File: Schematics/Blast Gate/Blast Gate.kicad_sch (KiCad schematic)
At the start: 14 parts

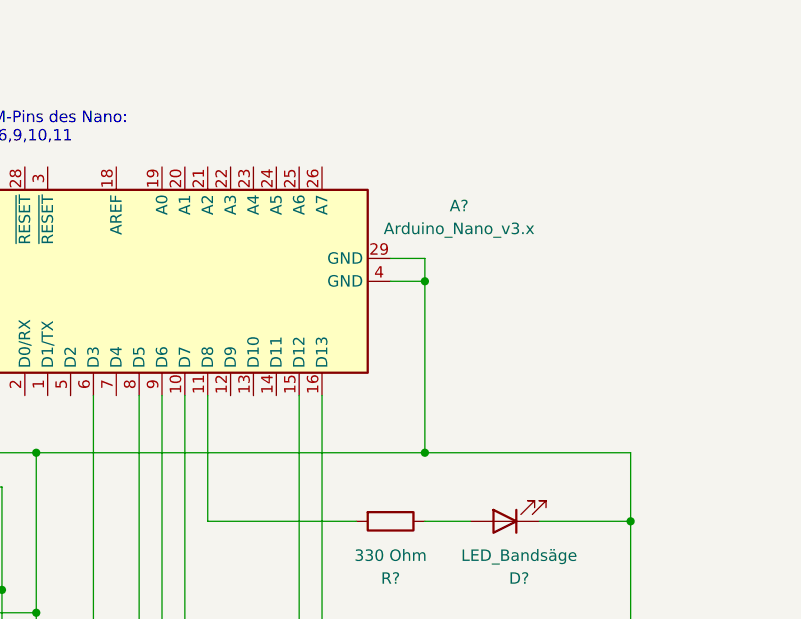
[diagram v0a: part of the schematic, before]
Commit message: Add buttons for open/close, introduced basic logic
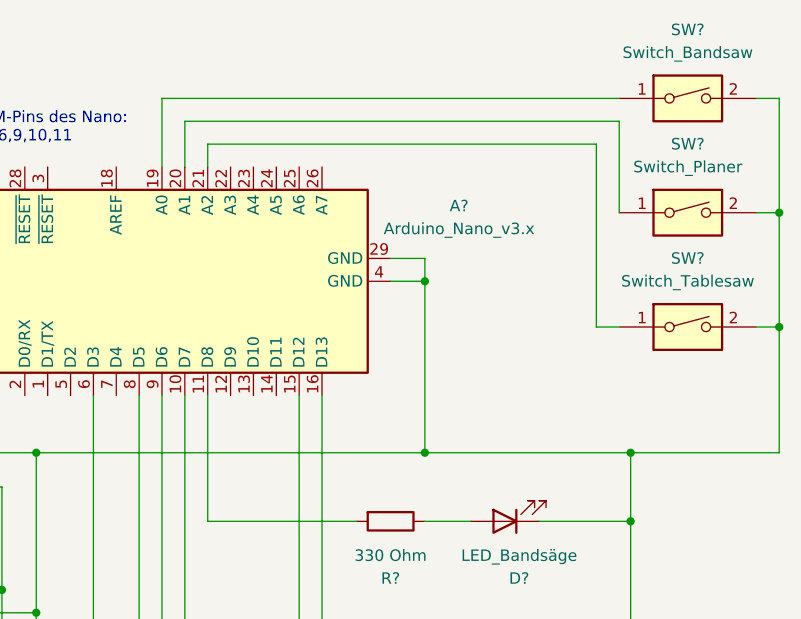
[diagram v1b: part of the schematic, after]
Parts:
- added SW?: Switch_Tablesaw, symbol Switch:SW_DIP_x01
- added SW?: Switch_Bandsaw, symbol Switch:SW_DIP_x01
- added SW?: Switch_Planer, symbol Switch:SW_DIP_x01
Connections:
- net GND: now also SW?.2, SW?.2, SW?.2
- net at A?.19 (A0): now also SW?.1
- net at A?.20 (A1): now also SW?.1
- net at A?.21 (A2): now also SW?.1
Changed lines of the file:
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@@
   (junction (at 86.36 107.95) (diameter 0) (color 0 0 0 0)
   )
+  (junction (at 168.91 48.26) (diameter 0) (color 0 0 0 0)
+  )
   (junction (at 55.88 52.07) (diameter 0) (color 0 0 0 0)
   )
@@
   (junction (at 41.91 104.14) (diameter 0) (color 0 0 0 0)
   )
+  (junction (at 168.91 35.56) (diameter 0) (color 0 0 0 0)
+  )
   (junction (at 82.55 105.41) (diameter 0) (color 0 0 0 0)
   )
+  (junction (at 152.4 62.23) (diameter 0) (color 0 0 0 0)
+  )
   (junction (at 86.36 80.01) (diameter 0) (color 0 0 0 0)
   )
@@
     (stroke (width 0) (type default) (color 0 0 0 0))
   )
+  (wire (pts (xy 100.33 30.48) (xy 100.33 22.86))
+    (stroke (width 0) (type default) (color 0 0 0 0))
+  )
   (wire (pts (xy 30.48 99.06) (xy 36.83 99.06))
     (stroke (width 0) (type default) (color 0 0 0 0))
@@
     (stroke (width 0) (type default) (color 0 0 0 0))
   )
+  (wire (pts (xy 168.91 62.23) (xy 152.4 62.23))
+    (stroke (width 0) (type default) (color 0 0 0 0))
+  )
   (wire (pts (xy 82.55 77.47) (xy 82.55 91.44))
     (stroke (width 0) (type default) (color 0 0 0 0))
@@
     (stroke (width 0) (type default) (color 0 0 0 0))
   )
+  (wire (pts (xy 166.37 48.26) (xy 168.91 48.26))
+    (stroke (width 0) (type default) (color 0 0 0 0))
+  )
   (wire (pts (xy 74.93 38.1) (xy 63.5 38.1))
     (stroke (width 0) (type default) (color 0 0 0 0))
@@
     (stroke (width 0) (type default) (color 0 0 0 0))
   )
+  (wire (pts (xy 168.91 48.26) (xy 168.91 62.23))
+    (stroke (width 0) (type default) (color 0 0 0 0))
+  )
   (wire (pts (xy 63.5 54.61) (xy 58.42 54.61))
     (stroke (width 0) (type default) (color 0 0 0 0))
@@
     (stroke (width 0) (type default) (color 0 0 0 0))
   )
+  (wire (pts (xy 151.13 25.4) (xy 151.13 35.56))
+    (stroke (width 0) (type default) (color 0 0 0 0))
+  )
   (wire (pts (xy 115.57 55.88) (xy 115.57 85.09))
     (stroke (width 0) (type default) (color 0 0 0 0))
@@
     (stroke (width 0) (type default) (color 0 0 0 0))
   )
+  (wire (pts (xy 102.87 25.4) (xy 151.13 25.4))
+    (stroke (width 0) (type default) (color 0 0 0 0))
+  )
   (wire (pts (xy 86.36 128.27) (xy 86.36 107.95))
     (stroke (width 0) (type default) (color 0 0 0 0))
   )
+  (wire (pts (xy 102.87 30.48) (xy 102.87 25.4))
+    (stroke (width 0) (type default) (color 0 0 0 0))
+  )
   (wire (pts (xy 82.55 77.47) (xy 82.55 66.04))
     (stroke (width 0) (type default) (color 0 0 0 0))
@@
     (stroke (width 0) (type default) (color 0 0 0 0))
   )
+  (wire (pts (xy 105.41 27.94) (xy 148.59 27.94))
+    (stroke (width 0) (type default) (color 0 0 0 0))
+  )
   (wire (pts (xy 152.4 85.09) (xy 152.4 69.85))
     (stroke (width 0) (type default) (color 0 0 0 0))
@@
     (stroke (width 0) (type default) (color 0 0 0 0))
   )
+  (wire (pts (xy 168.91 22.86) (xy 168.91 35.56))
+    (stroke (width 0) (type default) (color 0 0 0 0))
+  )
   (wire (pts (xy 142.24 69.85) (xy 152.4 69.85))
     (stroke (width 0) (type default) (color 0 0 0 0))
@@
     (stroke (width 0) (type default) (color 0 0 0 0))
   )
+  (wire (pts (xy 148.59 48.26) (xy 151.13 48.26))
+    (stroke (width 0) (type default) (color 0 0 0 0))
+  )
+  (wire (pts (xy 105.41 30.48) (xy 105.41 27.94))
+    (stroke (width 0) (type default) (color 0 0 0 0))
+  )
   (wire (pts (xy 78.74 80.01) (xy 86.36 80.01))
     (stroke (width 0) (type default) (color 0 0 0 0))
@@
     (stroke (width 0) (type default) (color 0 0 0 0))
   )
+  (wire (pts (xy 148.59 27.94) (xy 148.59 48.26))
+    (stroke (width 0) (type default) (color 0 0 0 0))
+  )
   (wire (pts (xy 54.61 52.07) (xy 55.88 52.07))
     (stroke (width 0) (type default) (color 0 0 0 0))
   )
+  (wire (pts (xy 100.33 22.86) (xy 151.13 22.86))
+    (stroke (width 0) (type default) (color 0 0 0 0))
+  )
   (wire (pts (xy 36.83 147.32) (xy 29.21 147.32))
     (stroke (width 0) (type default) (color 0 0 0 0))
@@
     (stroke (width 0) (type default) (color 0 0 0 0))
   )
+  (wire (pts (xy 168.91 35.56) (xy 168.91 48.26))
+    (stroke (width 0) (type default) (color 0 0 0 0))
+  )
   (wire (pts (xy 86.36 80.01) (xy 86.36 93.98))
     (stroke (width 0) (type default) (color 0 0 0 0))
   )
+  (wire (pts (xy 166.37 22.86) (xy 168.91 22.86))
+    (stroke (width 0) (type default) (color 0 0 0 0))
+  )
   (wire (pts (xy 92.71 82.55) (xy 78.74 82.55))
     (stroke (width 0) (type default) (color 0 0 0 0))
@@
   )
   (wire (pts (xy 30.48 101.6) (xy 39.37 101.6))
+    (stroke (width 0) (type default) (color 0 0 0 0))
+  )
+  (wire (pts (xy 166.37 35.56) (xy 168.91 35.56))
     (stroke (width 0) (type default) (color 0 0 0 0))
   )
@@
       (effects (font (size 1.27 1.27)) (justify left) hide)
     )
+  )
+  (symbol (lib_id "Switch:SW_DIP_x01") (at 158.75 48.26 0) (unit 1)
+    (in_bom yes) (on_board yes) (fields_autoplaced)
+    (property "Reference" "SW?" (id 0) (at 158.75 40.64 0))
+    (property "Value" "Switch_Tablesaw" (id 1) (at 158.75 43.18 0))
+    (property "Footprint" "" (id 2) (at 158.75 48.26 0)
+      (effects (font (size 1.27 1.27)) hide)
+    )
+    (property "Datasheet" "~" (id 3) (at 158.75 48.26 0)
+      (effects (font (size 1.27 1.27)) hide)
+    )
+    (pin "1")
+    (pin "2")
   )
   (symbol (lib_id "Connector:Conn_01x03_Male") (at 25.4 101.6 0) (unit 1)
@@
     (pin "2")
   )
+  (symbol (lib_id "Switch:SW_DIP_x01") (at 158.75 22.86 0) (unit 1)
+    (in_bom yes) (on_board yes) (fields_autoplaced)
+    (property "Reference" "SW?" (id 0) (at 158.75 15.24 0))
+    (property "Value" "Switch_Bandsaw" (id 1) (at 158.75 17.78 0))
+    (property "Footprint" "" (id 2) (at 158.75 22.86 0)
+      (effects (font (size 1.27 1.27)) hide)
+    )
+    (property "Datasheet" "~" (id 3) (at 158.75 22.86 0)
+      (effects (font (size 1.27 1.27)) hide)
+    )
+    (pin "1")
+    (pin "2")
+  )
   (symbol (lib_id "Connector:Conn_01x02_Male") (at 49.53 52.07 0) (unit 1)
     (in_bom yes) (on_board yes) (fields_autoplaced)
@@
     (pin "3")
   )
+  (symbol (lib_id "Switch:SW_DIP_x01") (at 158.75 35.56 0) (unit 1)
+    (in_bom yes) (on_board yes) (fields_autoplaced)
+    (property "Reference" "SW?" (id 0) (at 158.75 27.94 0))
+    (property "Value" "Switch_Planer" (id 1) (at 158.75 30.48 0))
+    (property "Footprint" "" (id 2) (at 158.75 35.56 0)
+      (effects (font (size 1.27 1.27)) hide)
+    )
+    (property "Datasheet" "~" (id 3) (at 158.75 35.56 0)
+      (effects (font (size 1.27 1.27)) hide)
+    )
+    (pin "1")
+    (pin "2")
+  )
   (sheet_instances
     (path "/" (page "1"))
@@
       (reference "R?") (unit 1) (value "330 Ohm") (footprint "")
     )
-  )
+    (path "/10456ba1-1522-4ac6-b240-9d1a9438165f"
+      (reference "SW?") (unit 1) (value "Switch_Tablesaw") (footprint "")
+    )
+    (path "/95d29c00-43a8-4b8b-ba8a-1c723fd3ede0"
+      (reference "SW?") (unit 1) (value "Switch_Bandsaw") (footprint "")
+    )
+    (path "/fdf9853a-92f9-4c86-9c98-dfd517dbcaed"
+      (reference "SW?") (unit 1) (value "Switch_Planer") (footprint "")
+    )
+  )
